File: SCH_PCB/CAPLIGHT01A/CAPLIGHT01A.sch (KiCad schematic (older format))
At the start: 29 parts, among them J1 JUMP_3X2, J10 JUMP_2x1, J11 JUMP_3X2, J12 CONN_2, J13 CONN_2, J2 CONN1_1, J3 CONN1_1, J4 CONN1_1, J5 CONN1_1, J6 CONN1_1, J7 CONN1_1, J8 CONN1_1, J9 JUMP_2x1, P1 USB_OTG, U1 LTC3625

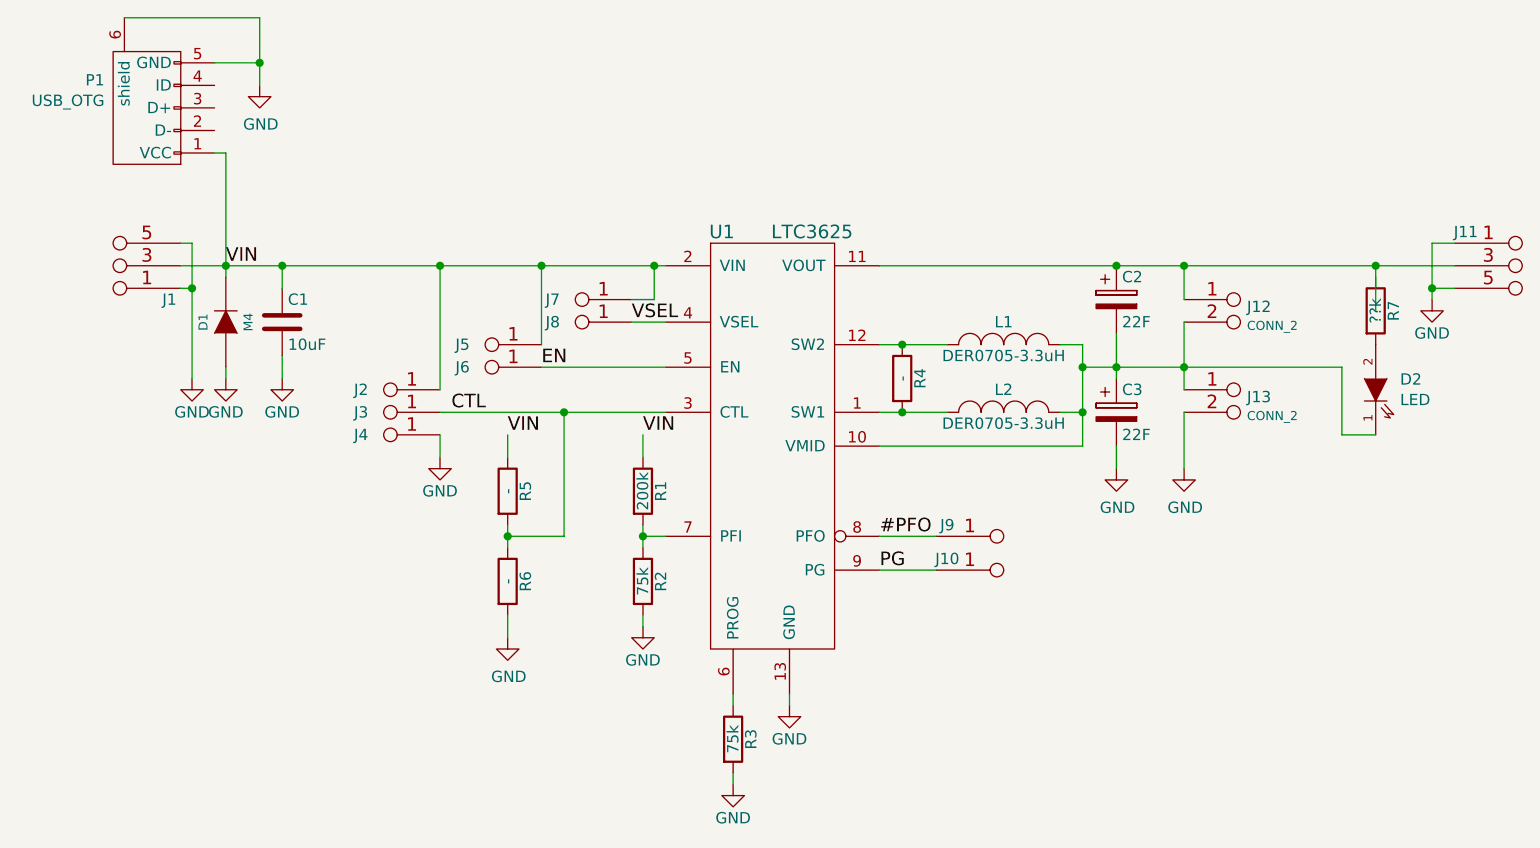
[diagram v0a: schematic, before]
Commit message: Second capacitor SMD pad
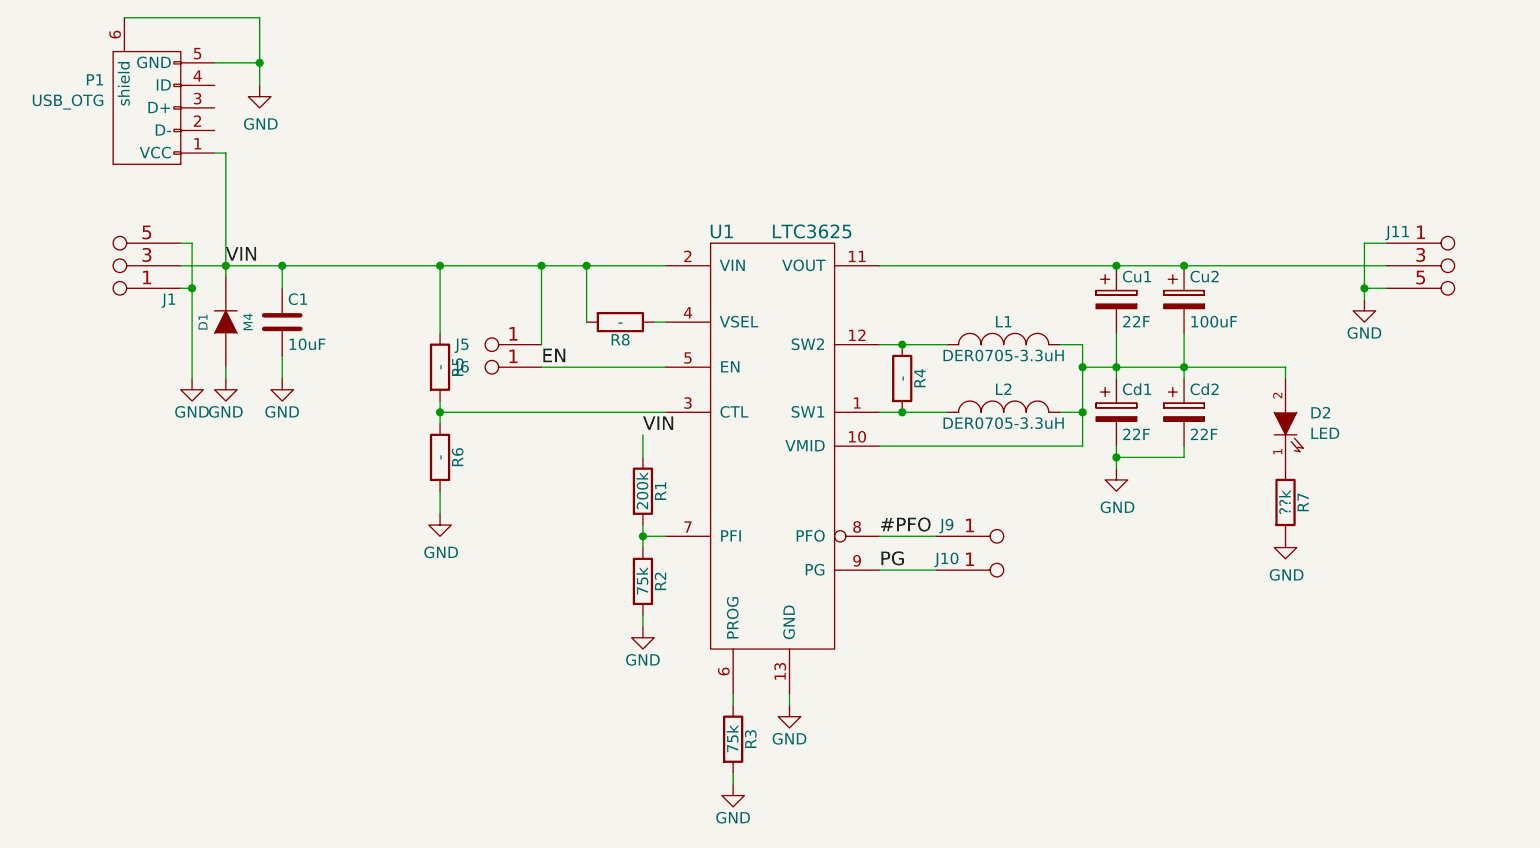
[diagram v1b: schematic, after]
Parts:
- removed J12: CONN_2, Mlab_C:C_Radial_D16_L25_P7.5, symbol CONN_2
- removed J13: CONN_2, Mlab_Pin_Headers:Straight_1x01, symbol CONN_2
- removed J2, J3, J4, J7, J8: CONN1_1, Mlab_Pin_Headers:Straight_1x01, symbol CONN1_1
- added Cd2: 22F, Mlab_C:C_Radial_D16_L25_P7.5, symbol CP
- added Cu2: 100uF, Mlab_C:SMD-0603, symbol CP
- added R8: -, Mlab_R:SMD-0805, symbol R
- renumbered C3 to Cd1, C2 to Cu1
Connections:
- net GND: now also R7.2, Cd2.2
- net VIN: now also R8.2
- net at Cd1.1, Cu1.2, L1.2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: now also D2.2 (A), Cd2.1, Cu2.2; no longer D2.1 (K)
- net at Cu1.1, J11.3 (4), J11.4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: now also Cu2.1
- net at R7.1: now also D2.1 (K)
- net CTL: no longer names the net of R5.2, R6.1, U1.3 (CTL)
- net VSEL: no longer names the net of U1.4 (VSEL)
- net VSEL: now also R8.1
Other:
- moved on the sheet: D2, J11, R5, R6, R7

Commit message: only for ExpaLight
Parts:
- removed Cd2: 22F, Mlab_C:C_Radial_D16_L25_P7.5, symbol CP
- removed Cu2: 100uF, Mlab_C:SMD-0603, symbol CP
- removed L2: DER0705-3.3uH, Mlab_L:DER0705, symbol INDUCTOR_SMALL
- removed R4, R5, R6: -, Mlab_R:SMD-0805, symbol R
- C2: renamed from Cu1; value 22F -> 100uF; footprint Mlab_C:C_Radial_D16_L25_P7.5 -> Mlab_C:TantalC_SizeC_Reflow
- C3: renamed from Cd1; footprint Mlab_C:C_Radial_D16_L25_P7.5 -> Mlab_C:C_Radial_D18_L25_P7.5
- R2: renamed from R1; value 200k -> 287k
- R3: renamed from R2; value 75k -> 100k
- R4: renamed from R3; value 75k -> 71.5k
- renumbered J5 to J2, J6 to J3, J9 to J4, J10 to J5, J11 to J6, R8 to R1, R7 to R5
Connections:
- net GND: now also D2.1 (K); no longer R5.2
- net VIN: now also U1.3 (CTL)
- net at U1.1 (SW1): now also L1.1, U1.12 (SW2)
- net at C2.2, C3.1, L1.2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: now also R5.1; no longer D2.2 (A)
- new net: D2.2 (A), R5.2
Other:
- moved on the sheet: D2, R5
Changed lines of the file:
@@
 $EndComp
 $Comp
-L CP Cd1
+L CP C3
 U 1 1 56E812E5
 P 7050 3650
-F 0 "Cd1" H 7075 3750 50  0000 L CNN
+F 0 "C3" H 7075 3750 50  0000 L CNN
 F 1 "22F" H 7075 3550 50  0000 L CNN
-F 2 "Mlab_C:C_Radial_D16_L25_P7.5" H 7088 3500 50  0001 C CNN
+F 2 "Mlab_C:C_Radial_D18_L25_P7.5" H 7088 3500 50  0001 C CNN
 F 3 "" H 7050 3650 50  0000 C CNN
 	1    7050 3650
@@
 $EndComp
 $Comp
-L CONN1_1 J6
+L CONN1_1 J3
 U 1 1 56E82602
 P 4200 3400
-F 0 "J6" H 4250 3450 50  0000 C CNN
+F 0 "J3" H 4250 3450 50  0000 C CNN
 F 1 "CONN1_1" H 4300 3350 40  0001 C CNN
 F 2 "Mlab_Pin_Headers:Straight_1x01" H 4250 3350 60  0001 C CNN
@@
 $EndComp
 $Comp
-L CONN1_1 J5
+L CONN1_1 J2
 U 1 1 56E82658
 P 4200 3300
-F 0 "J5" H 4250 3350 50  0000 C CNN
+F 0 "J2" H 4250 3350 50  0000 C CNN
 F 1 "CONN1_1" H 4300 3250 40  0001 C CNN
 F 2 "Mlab_Pin_Headers:Straight_1x01" H 4250 3250 60  0001 C CNN
@@
 VIN
 $Comp
-L R R2
+L R R3
 U 1 1 56E84F85
 P 4950 4400
-F 0 "R2" V 5030 4400 50  0000 C CNN
-F 1 "75k" V 4950 4400 50  0000 C CNN
+F 0 "R3" H 4881 4446 50  0000 R CNN
+F 1 "100k" H 4881 4355 50  0000 R CNN
 F 2 "Mlab_R:SMD-0805" V 4880 4400 50  0001 C CNN
 F 3 "" H 4950 4400 50  0000 C CNN
@@
 $EndComp
 $Comp
-L R R1
+L R R2
 U 1 1 56E85082
 P 4950 4000
-F 0 "R1" V 5030 4000 50  0000 C CNN
-F 1 "200k" V 4950 4000 50  0000 C CNN
+F 0 "R2" V 5030 4000 50  0000 C CNN
+F 1 "287k" V 4950 4000 50  0000 C CNN
 F 2 "Mlab_R:SMD-0805" V 4880 4000 50  0001 C CNN
 F 3 "" H 4950 4000 50  0000 C CNN
@@
 Connection ~ 4950 4200
 $Comp
-L R R3
+L R R4
 U 1 1 56E85E42
 P 5350 5100
-F 0 "R3" V 5430 5100 50  0000 C CNN
-F 1 "75k" V 5350 5100 50  0000 C CNN
+F 0 "R4" V 5430 5100 50  0000 C CNN
+F 1 "71.5k" V 5350 5100 50  0000 C CNN
 F 2 "Mlab_R:SMD-0805" V 5280 5100 50  0001 C CNN
 F 3 "" H 5350 5100 50  0000 C CNN
@@
 $EndComp
 $Comp
-L INDUCTOR_SMALL L2
-U 1 1 56E87295
-P 6550 3650
-F 0 "L2" H 6550 3750 50  0000 C CNN
-F 1 "DER0705-3.3uH" H 6550 3600 50  0000 C CNN
-F 2 "Mlab_L:DER0705" H 6550 3650 50  0001 C CNN
-F 3 "" H 6550 3650 50  0000 C CNN
-	1    6550 3650
-	1    0    0    -1
-$EndComp
-$Comp
-L CP Cu1
+L CP C2
 U 1 1 56E875AF
 P 7050 3150
-F 0 "Cu1" H 7075 3250 50  0000 L CNN
-F 1 "22F" H 7075 3050 50  0000 L CNN
-F 2 "Mlab_C:C_Radial_D16_L25_P7.5" H 7088 3000 50  0001 C CNN
+F 0 "C2" H 7075 3250 50  0000 L CNN
+F 1 "100uF" H 7075 3050 50  0000 L CNN
+F 2 "Mlab_C:TantalC_SizeC_Reflow" H 7088 3000 50  0001 C CNN
 F 3 "" H 7050 3150 50  0000 C CNN
 	1    7050 3150
 	1    0    0    -1
 $EndComp
-$Comp
-L R R4
-U 1 1 56E8835F
-P 6100 3500
-F 0 "R4" V 6180 3500 50  0000 C CNN
-F 1 "-" V 6100 3500 50  0000 C CNN
-F 2 "Mlab_R:SMD-0805" V 6030 3500 50  0001 C CNN
-F 3 "" H 6100 3500 50  0000 C CNN
-	1    6100 3500
-	1    0    0    -1
-$EndComp
-Wire Wire Line
-	6000 3650 6300 3650
 Wire Wire Line
 	6000 3350 6300 3350
-Connection ~ 6100 3350
-Connection ~ 6100 3650
 Wire Wire Line
 	6800 3350 6900 3350
 Wire Wire Line
 	6900 3350 6900 3800
-Wire Wire Line
-	6900 3650 6800 3650
 Connection ~ 6900 3450
 Wire Wire Line
@@
 Wire Wire Line
 	6900 3800 6000 3800
-Connection ~ 6900 3650
-$Comp
-L JUMP_2x1 J9
+$Comp
+L JUMP_2x1 J4
 U 1 1 56E8A378
 P 6650 4350
-F 0 "J9" H 6300 4550 50  0000 C CNN
+F 0 "J4" H 6300 4550 50  0000 C CNN
 F 1 "JUMP_2x1" V 6650 4500 40  0001 C CNN
 F 2 "Mlab_Pin_Headers:Straight_2x01" H 6650 4350 60  0001 C CNN
@@
 PG
 $Comp
-L JUMP_3X2 J11
+L JUMP_3X2 J6
 U 1 1 56E8C89C
 P 8650 3050
-F 0 "J11" H 8300 3250 50  0000 C CNN
+F 0 "J6" H 8300 3250 50  0000 C CNN
 F 1 "JUMP_3X2" V 8650 3100 40  0001 C CNN
 F 2 "Mlab_Pin_Headers:Straight_2x03" H 8650 3050 60  0001 C CNN
@@
 L LED D2
 U 1 1 5771A40B
-P 7800 3700
-F 0 "D2" V 7846 3592 50  0000 R CNN
-F 1 "LED" V 7755 3592 50  0000 R CNN
-F 2 "Mlab_Pin_Headers:Straight_1x02" H 7800 3700 50  0001 C CNN
-F 3 "" H 7800 3700 50  0000 C CNN
-	1    7800 3700
+P 7550 4000
+F 0 "D2" V 7596 3892 50  0000 R CNN
+F 1 "LED" V 7505 3892 50  0000 R CNN
+F 2 "Mlab_Pin_Headers:Straight_1x02" H 7550 4000 50  0001 C CNN
+F 3 "" H 7550 4000 50  0000 C CNN
+	1    7550 4000
 	0    -1   -1   0
 $EndComp
-Wire Wire Line
-	4050 3700 4050 3600
-Connection ~ 4050 3650
+$Comp
+L R R5
+U 1 1 57726713
+P 7550 3650
+F 0 "R5" V 7630 3650 50  0000 C CNN
+F 1 "??k" V 7550 3650 50  0000 C CNN
+F 2 "Mlab_R:SMD-0805" V 7480 3650 50  0001 C CNN
+F 3 "" H 7550 3650 50  0000 C CNN
+	1    7550 3650
+	1    0    0    -1
+$EndComp
 $Comp
 L GND #PWR09
-U 1 1 57725BCB
-P 4050 4100
-F 0 "#PWR09" H 4050 3850 50  0001 C CNN
-F 1 "GND" H 4055 3927 50  0000 C CNN
-F 2 "" H 4050 4100 50  0000 C CNN
-F 3 "" H 4050 4100 50  0000 C CNN
-	1    4050 4100
-	1    0    0    -1
-$EndComp
-Wire Wire Line
-	4050 3000 4050 3300
-Wire Wire Line
-	4050 4100 4050 4000
-$Comp
-L R R5
-U 1 1 57726401
-P 4050 3450
-F 0 "R5" V 4130 3450 50  0000 C CNN
-F 1 "-" V 4050 3450 50  0000 C CNN
-F 2 "Mlab_R:SMD-0805" V 3980 3450 50  0001 C CNN
-F 3 "" H 4050 3450 50  0000 C CNN
-	1    4050 3450
-	1    0    0    -1
-$EndComp
-$Comp
-L R R6
-U 1 1 5772661C
-P 4050 3850
-F 0 "R6" V 4130 3850 50  0000 C CNN
-F 1 "-" V 4050 3850 50  0000 C CNN
-F 2 "Mlab_R:SMD-0805" V 3980 3850 50  0001 C CNN
-F 3 "" H 4050 3850 50  0000 C CNN
-	1    4050 3850
-	1    0    0    -1
-$EndComp
-$Comp
-L R R7
-U 1 1 57726713
-P 7800 4050
-F 0 "R7" V 7880 4050 50  0000 C CNN
-F 1 "??k" V 7800 4050 50  0000 C CNN
-F 2 "Mlab_R:SMD-0805" V 7730 4050 50  0001 C CNN
-F 3 "" H 7800 4050 50  0000 C CNN
-	1    7800 4050
-	1    0    0    -1
-$EndComp
-Connection ~ 7350 3450
-$Comp
-L GND #PWR010
 U 1 1 57728495
 P 7050 3900
-F 0 "#PWR010" H 7050 3650 50  0001 C CNN
+F 0 "#PWR09" H 7050 3650 50  0001 C CNN
 F 1 "GND" H 7055 3727 50  0000 C CNN
 F 2 "" H 7050 3900 50  0000 C CNN
@@
 	7050 3900 7050 3800
 $Comp
-L GND #PWR011
+L GND #PWR010
 U 1 1 5776E87A
-P 7800 4200
-F 0 "#PWR011" H 7800 3950 50  0001 C CNN
-F 1 "GND" H 7805 4027 50  0000 C CNN
-F 2 "" H 7800 4200 50  0000 C CNN
-F 3 "" H 7800 4200 50  0000 C CNN
-	1    7800 4200
-	1    0    0    -1
-$EndComp
-Wire Wire Line
-	7050 3850 7350 3850
-Connection ~ 7050 3850
-$Comp
-L CP Cu2
-U 1 1 57778D7A
-P 7350 3150
-F 0 "Cu2" H 7375 3250 50  0000 L CNN
-F 1 "100uF" H 7375 3050 50  0000 L CNN
-F 2 "Mlab_C:SMD-0603" H 7388 3000 50  0001 C CNN
-F 3 "" H 7350 3150 50  0000 C CNN
-	1    7350 3150
-	1    0    0    -1
-$EndComp
-$Comp
-L CP Cd2
-U 1 1 57778DEE
-P 7350 3650
-F 0 "Cd2" H 7375 3750 50  0000 L CNN
-F 1 "22F" H 7375 3550 50  0000 L CNN
-F 2 "Mlab_C:C_Radial_D16_L25_P7.5" H 7388 3500 50  0001 C CNN
-F 3 "" H 7350 3650 50  0000 C CNN
-	1    7350 3650
-	1    0    0    -1
-$EndComp
-Wire Wire Line
-	7350 3300 7350 3500
-Wire Wire Line
-	7350 3850 7350 3800
-Connection ~ 7350 3000
-$Comp
-L JUMP_2x1 J10
+P 7550 4200
+F 0 "#PWR010" H 7550 3950 50  0001 C CNN
+F 1 "GND" H 7555 4027 50  0000 C CNN
+F 2 "" H 7550 4200 50  0000 C CNN
+F 3 "" H 7550 4200 50  0000 C CNN
+	1    7550 4200
+	1    0    0    -1
+$EndComp
+$Comp
+L JUMP_2x1 J5
 U 1 1 56E8A461
 P 6650 4500
-F 0 "J10" H 6300 4700 50  0000 C CNN
+F 0 "J5" H 6300 4700 50  0000 C CNN
 F 1 "JUMP_2x1" V 6650 4650 40  0001 C CNN
 F 2 "Mlab_Pin_Headers:Straight_2x01" H 6650 4500 60  0001 C CNN
@@
 	1    0    0    -1
 $EndComp
-Wire Wire Line
-	6900 3450 7800 3450
-Wire Wire Line
-	7800 3450 7800 3500
 Wire Wire Line
 	6000 3000 8250 3000
@@
 	5050 3650 4050 3650
 $Comp
-L R R8
+L R R1
 U 1 1 57779A79
 P 4850 3250
-F 0 "R8" V 4930 3250 50  0000 C CNN
+F 0 "R1" V 4930 3250 50  0000 C CNN
 F 1 "-" V 4850 3250 50  0000 C CNN
 F 2 "Mlab_R:SMD-0805" V 4780 3250 50  0001 C CNN
@@
 	4700 3250 4700 3000
 Connection ~ 4700 3000
+Wire Wire Line
+	6900 3450 7550 3450
+Wire Wire Line
+	7550 3450 7550 3500
+Wire Wire Line
+	4050 3650 4050 3000
+Wire Wire Line
+	6000 3650 6000 3350
+Connection ~ 6000 3350
 $EndSCHEMATC

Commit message: layout edit
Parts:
- removed J2: CONN1_1, Mlab_Pin_Headers:Straight_1x01, symbol CONN1_1
- removed J4, J5: JUMP_2x1, Mlab_Pin_Headers:Straight_2x01, symbol JUMP_2x1
- removed J6: JUMP_3X2, Mlab_Pin_Headers:Straight_2x03, symbol JUMP_3X2
- added J3: JUMP_2x1, Measurement_Points:Measurement_Point_Round-SMD-Pad_Small, symbol JUMP_2x1
- J2: renamed from J3; footprint Mlab_Pin_Headers:Straight_1x01 -> Measurement_Points:Measurement_Point_Round-SMD-Pad_Small
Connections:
- net #PFO: now also J3.1, J3.2 (1)
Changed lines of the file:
@@
 $EndComp
 $Comp
-L CONN1_1 J3
+L CONN1_1 J2
 U 1 1 56E82602
 P 4200 3400
-F 0 "J3" H 4250 3450 50  0000 C CNN
+F 0 "J2" H 4250 3450 50  0000 C CNN
 F 1 "CONN1_1" H 4300 3350 40  0001 C CNN
-F 2 "Mlab_Pin_Headers:Straight_1x01" H 4250 3350 60  0001 C CNN
+F 2 "Measurement_Points:Measurement_Point_Round-SMD-Pad_Small" H 4250 3350 60  0001 C CNN
 F 3 "" H 4250 3350 60  0000 C CNN
 	1    4200 3400
-	-1   0    0    1
-$EndComp
-$Comp
-L CONN1_1 J2
-U 1 1 56E82658
-P 4200 3300
-F 0 "J2" H 4250 3350 50  0000 C CNN
-F 1 "CONN1_1" H 4300 3250 40  0001 C CNN
-F 2 "Mlab_Pin_Headers:Straight_1x01" H 4250 3250 60  0001 C CNN
-F 3 "" H 4250 3250 60  0000 C CNN
-	1    4200 3300
 	-1   0    0    1
 $EndComp
@@
 $EndComp
 Connection ~ 4050 3000
-Wire Wire Line
-	4500 3350 4500 3000
-Connection ~ 4500 3000
 Text Label 4500 3450 0    60   ~ 0
 EN
@@
 Wire Wire Line
 	6900 3800 6000 3800
-$Comp
-L JUMP_2x1 J4
-U 1 1 56E8A378
-P 6650 4350
-F 0 "J4" H 6300 4550 50  0000 C CNN
-F 1 "JUMP_2x1" V 6650 4500 40  0001 C CNN
-F 2 "Mlab_Pin_Headers:Straight_2x01" H 6650 4350 60  0001 C CNN
-F 3 "" H 6650 4350 60  0000 C CNN
-	1    6650 4350
-	1    0    0    -1
-$EndComp
 Wire Wire Line
 	6000 4200 6250 4200
-Wire Wire Line
-	6000 4350 6250 4350
 Text Label 6000 4200 0    60   ~ 0
 #PFO
 Text Label 6000 4350 0    60   ~ 0
 PG
-$Comp
-L JUMP_3X2 J6
-U 1 1 56E8C89C
-P 8650 3050
-F 0 "J6" H 8300 3250 50  0000 C CNN
-F 1 "JUMP_3X2" V 8650 3100 40  0001 C CNN
-F 2 "Mlab_Pin_Headers:Straight_2x03" H 8650 3050 60  0001 C CNN
-F 3 "" H 8650 3050 60  0000 C CNN
-	1    8650 3050
-	1    0    0    -1
-$EndComp
-Connection ~ 7050 3000
-$Comp
-L GND #PWR07
-U 1 1 56E8CF84
-P 8150 3150
-F 0 "#PWR07" H 8150 2900 50  0001 C CNN
-F 1 "GND" H 8150 3000 50  0000 C CNN
-F 2 "" H 8150 3150 50  0000 C CNN
-F 3 "" H 8150 3150 50  0000 C CNN
-	1    8150 3150
-	1    0    0    -1
-$EndComp
-Wire Wire Line
-	8250 2900 8150 2900
-Wire Wire Line
-	8150 2900 8150 3150
-Wire Wire Line
-	8250 3100 8150 3100
-Connection ~ 8150 3100
 Wire Wire Line
 	3100 2500 3100 3050
@@
 	3050 2500 3100 2500
 $Comp
-L GND #PWR08
+L GND #PWR07
 U 1 1 5771AF62
 P 3250 2200
-F 0 "#PWR08" H 3250 1950 50  0001 C CNN
+F 0 "#PWR07" H 3250 1950 50  0001 C CNN
 F 1 "GND" H 3255 2027 50  0000 C CNN
 F 2 "" H 3250 2200 50  0000 C CNN
@@
 $EndComp
 $Comp
-L GND #PWR09
+L GND #PWR08
 U 1 1 57728495
 P 7050 3900
-F 0 "#PWR09" H 7050 3650 50  0001 C CNN
+F 0 "#PWR08" H 7050 3650 50  0001 C CNN
 F 1 "GND" H 7055 3727 50  0000 C CNN
 F 2 "" H 7050 3900 50  0000 C CNN
@@
 	7050 3900 7050 3800
 $Comp
-L GND #PWR010
+L GND #PWR09
 U 1 1 5776E87A
 P 7550 4200
-F 0 "#PWR010" H 7550 3950 50  0001 C CNN
+F 0 "#PWR09" H 7550 3950 50  0001 C CNN
 F 1 "GND" H 7555 4027 50  0000 C CNN
 F 2 "" H 7550 4200 50  0000 C CNN
@@
 	1    0    0    -1
 $EndComp
-$Comp
-L JUMP_2x1 J5
-U 1 1 56E8A461
-P 6650 4500
-F 0 "J5" H 6300 4700 50  0000 C CNN
-F 1 "JUMP_2x1" V 6650 4650 40  0001 C CNN
-F 2 "Mlab_Pin_Headers:Straight_2x01" H 6650 4500 60  0001 C CNN
-F 3 "" H 6650 4500 60  0000 C CNN
-	1    6650 4500
-	1    0    0    -1
-$EndComp
-Wire Wire Line
-	6000 3000 8250 3000
 $Comp
 L LTC3625 U1
@@
 	6000 3650 6000 3350
 Connection ~ 6000 3350
+$Comp
+L JUMP_2x1 J3
+U 1 1 57791ABD
+P 6650 4350
+F 0 "J3" H 6300 4550 50  0000 C CNN
+F 1 "JUMP_2x1" V 6650 4500 40  0001 C CNN
+F 2 "Measurement_Points:Measurement_Point_Round-SMD-Pad_Small" H 6650 4350 60  0001 C CNN
+F 3 "" H 6650 4350 60  0000 C CNN
+	1    6650 4350
+	1    0    0    -1
+$EndComp
+Wire Wire Line
+	7050 3000 6000 3000
 $EndSCHEMATC
